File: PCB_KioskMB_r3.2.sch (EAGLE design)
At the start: 339 parts, among them IC1 ISL60002DIH325Z-TK, IC18 FT232RL, IC19 MCP6022-I/ST, IC2 SN65HVD12D, IC20 LTC1771EMS8, IC21 LTC1771EMS8, IC3 PIC24FJ256GA110-I/PT, IC4 PIC10F200T-I/OT, IC5 LM75ADP, IC6 24LC32A-I/MS, IC7 PCF2123TS/1-T, IC8 M25P16-VMN6P, IC9 LM3405AXMK/NOPB, J1 DF11-10DP-2DSA(01), J10 CCM03-3504LFT-NR, J13 3-641215-3, J14 3-641215-2, J15 3-641215-4, J16 3-641215-4, J40 DNP, J43 3-641215-4, J44 3-641215-4, J45 3-641215-4, J46 3-641215-5, J47 DF11-10DP-2DSA(01), J48 3-641215-2, J49 3-641215-2, J5 3-641215-2, J6 3-641215-2, J7 SS-6566-NF, J8 TSW-108-07-G-D, J9 SS-6566-NF, Q1 SSM6P49NU,LFPZ, Q14 TSM9938HEUK+T, Q15 SI4564DY, Q16 CSD87331Q3D, Q17 TSM9938HEUK+T, Q18 SI4564DY, Q19 CSD87331Q3D, Q2 FDC6330L, Q20 IPD30N06S2L-23, Q21 IPD30N06S2L-23, Q22 FDN352AP, Q23 FDN352AP, Q24 BSS138, Q3 SR3.3.TCT, Q4 7B-28.63636MAAJ-T, Q5 FDC6324L, Q6 CM519 32.768KDZF-UT, Q7 SSM6P49NU,LFPZ, Q8 IPD30N06S2L-23, Q9 IPD30N06S2L-23, U1 LTC1955, U2 HRXL-MAXSONAR-WRC-MB7387, U3 ADS1015, U6 TPS43061, U7 TPS43061, U8 TPA3111D1PWP, U9 OPA322SAIDBVT, X1 FH12-10S-0.5S1.00MM

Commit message: cleaned up silk
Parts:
- added FID3: (no value), technol:REF
- renumbered F1 to FID1, F2 to FID2
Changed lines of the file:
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@@
 <part name="C12" library="DISCRETE" deviceset="C-0603" device="" value="10nF"/>
 <part name="C13" library="DISCRETE" deviceset="C-0603" device="" value="10nF"/>
-<part name="F1" library="technol" deviceset="REF" device=""/>
-<part name="F2" library="technol" deviceset="REF" device=""/>
+<part name="FID1" library="technol" deviceset="REF" device=""/>
+<part name="FID2" library="technol" deviceset="REF" device=""/>
 <part name="C14" library="DISCRETE" deviceset="C-0603" device="" value="1u/6.3V"/>
 <part name="IC2" library="TexasInstruments-AON" deviceset="SN65HVD3082E" device="D" value="SN65HVD12D"/>
@@
 <part name="R35" library="DISCRETE" deviceset="R-0603" device="" value="3k"/>
 <part name="R36" library="DISCRETE" deviceset="R-0603" device="" value="1k"/>
+<part name="FID3" library="technol" deviceset="REF" device=""/>
 </parts>
 <sheets>
@@
 <attribute name="VALUE" x="67.6275" y="311.15" size="1.524" layer="96"/>
 </instance>
-<instance part="F1" gate="G$1" x="454.66" y="45.72" smashed="yes">
+<instance part="FID1" gate="G$1" x="454.66" y="45.72" smashed="yes">
 <attribute name="NAME" x="453.39" y="44.45" size="1.778" layer="95"/>
 </instance>
-<instance part="F2" gate="G$1" x="469.9" y="45.72" smashed="yes">
+<instance part="FID2" gate="G$1" x="469.9" y="45.72" smashed="yes">
 <attribute name="NAME" x="466.09" y="44.45" size="1.778" layer="95"/>
 </instance>
@@
 <instance part="X1" gate="-10" x="327.66" y="208.28"/>
 <instance part="U$90" gate="G$1" x="307.34" y="208.28" smashed="yes"/>
+<instance part="FID3" gate="G$1" x="469.9" y="53.34" smashed="yes">
+<attribute name="NAME" x="466.09" y="52.07" size="1.778" layer="95"/>
+</instance>
 </instances>
 <busses>

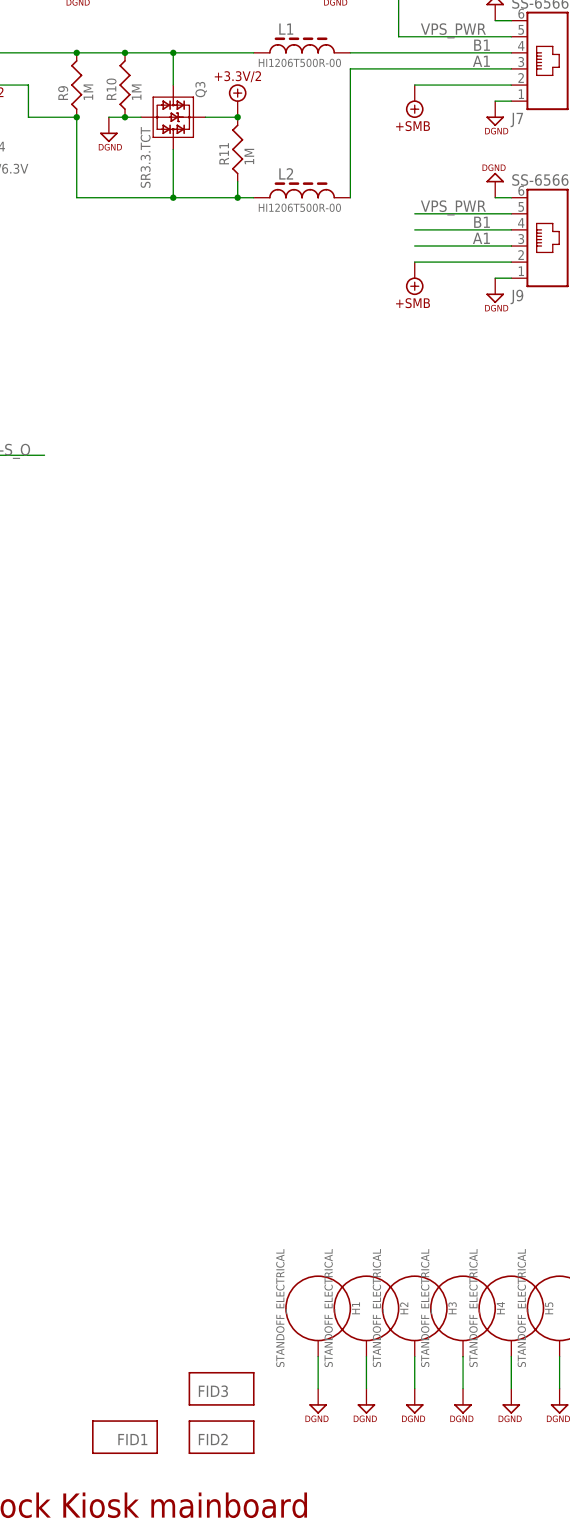
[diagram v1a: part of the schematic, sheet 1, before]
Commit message: added components ( for sbc power) and updated lan components.
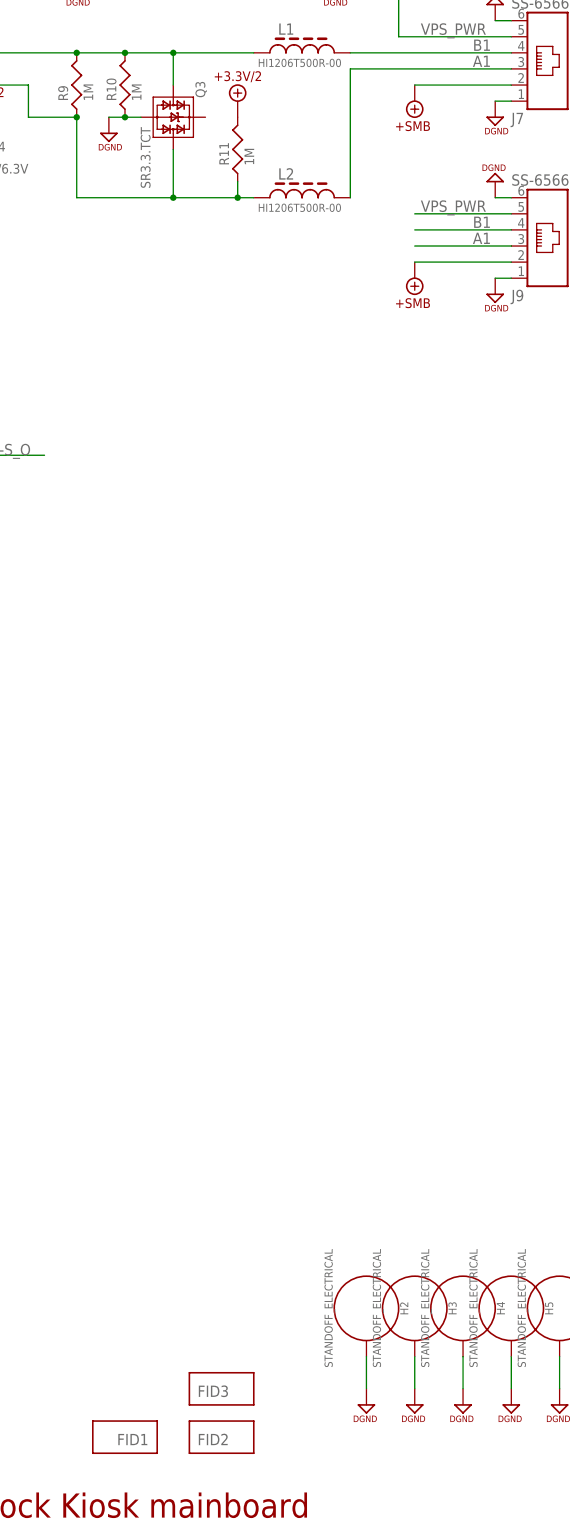
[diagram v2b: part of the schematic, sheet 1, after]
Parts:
- removed H1: STANDOFF_ELECTRICAL, SparkFun-Hardware:STANDOFF_ELECTRICAL
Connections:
- net +3.3V/2: no longer Q3.4
- net DGND: no longer H1.P$1
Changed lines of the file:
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@@
 <part name="U$34" library="SUPPLY" deviceset="+3.3V/1" device=""/>
 <part name="U$115" library="SUPPLY" deviceset="DGND" device=""/>
-<part name="U$5" library="SUPPLY" deviceset="DGND" device=""/>
 <part name="U$61" library="SUPPLY" deviceset="DGND" device=""/>
 <part name="U$122" library="SUPPLY" deviceset="DGND" device=""/>
@@
 <part name="U$86" library="SUPPLY" deviceset="DGND" device=""/>
 <part name="U$89" library="SUPPLY" deviceset="DGND" device=""/>
-<part name="H1" library="SparkFun-Hardware" deviceset="STANDOFF_ELECTRICAL" device=""/>
 <part name="H2" library="SparkFun-Hardware" deviceset="STANDOFF_ELECTRICAL" device=""/>
 <part name="H3" library="SparkFun-Hardware" deviceset="STANDOFF_ELECTRICAL" device=""/>
@@
 <instance part="U$34" gate="G$1" x="208.28" y="111.76" smashed="yes"/>
 <instance part="U$115" gate="G$1" x="15.24" y="48.26" smashed="yes"/>
-<instance part="U$5" gate="G$1" x="485.14" y="50.8" smashed="yes" rot="MR0"/>
 <instance part="U$61" gate="G$1" x="492.76" y="50.8" smashed="yes" rot="MR0"/>
 <instance part="U$122" gate="G$1" x="29.21" y="307.34" smashed="yes"/>
@@
 <instance part="U$86" gate="G$1" x="508" y="50.8" smashed="yes" rot="MR0"/>
 <instance part="U$89" gate="G$1" x="523.24" y="50.8" smashed="yes" rot="MR0"/>
-<instance part="H1" gate="G$1" x="485.14" y="66.04" rot="R270"/>
 <instance part="H2" gate="G$1" x="492.76" y="66.04" rot="R270"/>
 <instance part="H3" gate="G$1" x="500.38" y="66.04" rot="R270"/>
@@
 </segment>
 <segment>
-<pinref part="U$5" gate="G$1" pin="DGND"/>
-<pinref part="H1" gate="G$1" pin="P$1"/>
-<wire x1="485.14" y1="58.42" x2="485.14" y2="53.34" width="0.1524" layer="91"/>
-</segment>
-<segment>
 <pinref part="U$61" gate="G$1" pin="DGND"/>
 <pinref part="H2" gate="G$1" pin="P$1"/>
@@
 </segment>
 <segment>
-<wire x1="472.44" y1="254" x2="467.36" y2="254" width="0.1524" layer="91"/>
-<pinref part="Q3" gate="G$1" pin="4"/>
 <pinref part="U$159" gate="A" pin="+3.3V/2"/>
 <pinref part="R11" gate="G$1" pin="2"/>
-<junction x="472.44" y="254"/>
-</segment>
-<segment>
+</segment>
+<segment>
